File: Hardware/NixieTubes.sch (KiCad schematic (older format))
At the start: 14 parts, among them U1 HV5530, U2 HV5530

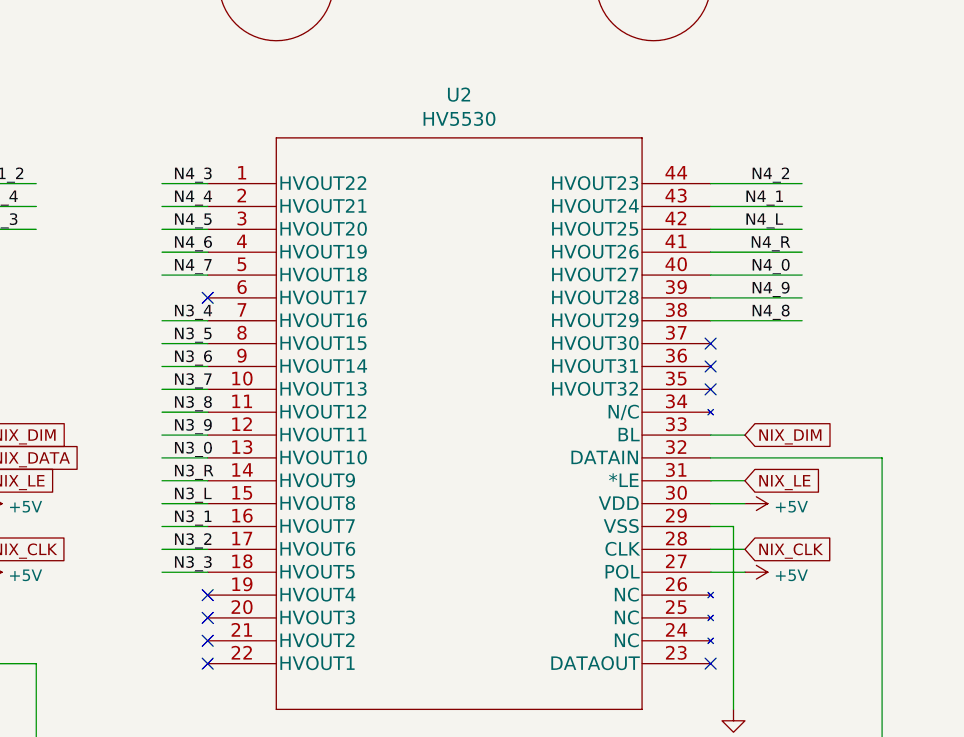
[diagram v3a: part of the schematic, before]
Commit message: Routed right nixies
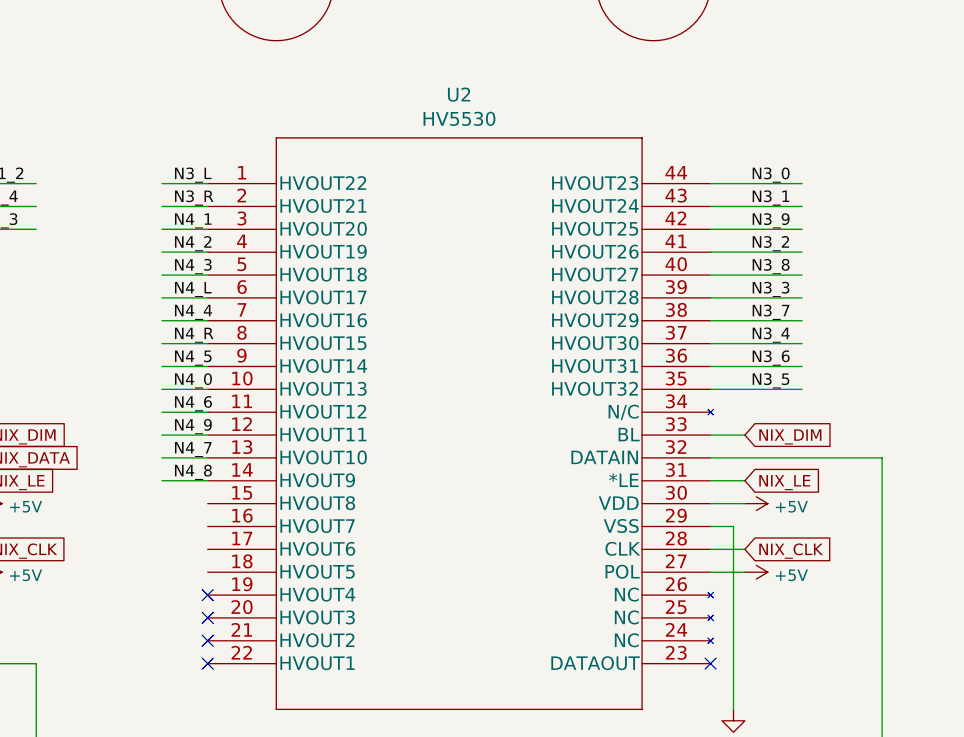
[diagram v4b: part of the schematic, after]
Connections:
- no-connect marks 16 -> 12
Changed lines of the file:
@@
 Wire Wire Line
 	7000 1400 7050 1400
-Wire Wire Line
-	4500 4000 4300 4000
-Wire Wire Line
-	4500 3900 4300 3900
-Wire Wire Line
-	4500 3800 4300 3800
-Wire Wire Line
-	4500 3700 4300 3700
-Wire Wire Line
-	4500 3600 4300 3600
-Wire Wire Line
-	4500 3500 4300 3500
-Wire Wire Line
-	4500 3400 4300 3400
-Wire Wire Line
-	4500 3300 4300 3300
-Wire Wire Line
-	4500 4400 4300 4400
-Wire Wire Line
-	4500 4300 4300 4300
-Wire Wire Line
-	4500 4200 4300 4200
-Wire Wire Line
-	4300 4100 4500 4100
-Text Label 4350 4100 0    50   ~ 0
-N3_L
-Text Label 4350 4200 0    50   ~ 0
-N3_1
-Text Label 4350 4300 0    50   ~ 0
+Text Label 7050 2700 2    50   ~ 0
+N3_0
+Text Label 7050 3300 2    50   ~ 0
+N3_7
+Text Label 7050 3200 2    50   ~ 0
+N3_3
+Text Label 7050 3100 2    50   ~ 0
+N3_8
+Text Label 7050 3000 2    50   ~ 0
 N3_2
-Text Label 4350 4400 0    50   ~ 0
-N3_3
-Text Label 4350 3300 0    50   ~ 0
-N3_4
-Text Label 4350 3400 0    50   ~ 0
-N3_5
-Text Label 4350 3500 0    50   ~ 0
-N3_6
-Text Label 4350 3600 0    50   ~ 0
-N3_7
-Text Label 4350 3700 0    50   ~ 0
-N3_8
-Text Label 4350 3800 0    50   ~ 0
-N3_9
-Text Label 4350 3900 0    50   ~ 0
-N3_0
-Text Label 4350 4000 0    50   ~ 0
-N3_R
-Text Label 7050 2700 2    50   ~ 0
-N4_2
-Text Label 4350 2700 0    50   ~ 0
-N4_3
-Text Label 4350 2800 0    50   ~ 0
-N4_4
-Text Label 4350 2900 0    50   ~ 0
-N4_5
-Text Label 4350 3000 0    50   ~ 0
-N4_6
-Text Label 4350 3100 0    50   ~ 0
-N4_7
-Text Label 7050 3300 2    50   ~ 0
-N4_8
-Text Label 7050 3200 2    50   ~ 0
-N4_9
-Text Label 7050 3100 2    50   ~ 0
-N4_0
-Text Label 7050 3000 2    50   ~ 0
-N4_R
-Text Label 6850 2800 0    50   ~ 0
-N4_1
-Text Label 6850 2900 0    50   ~ 0
-N4_L
-Wire Wire Line
-	6700 2900 7100 2900
-Wire Wire Line
-	6700 2800 7100 2800
 Wire Wire Line
 	6700 3200 7100 3200
 Wire Wire Line
 	6700 3300 7100 3300
-Wire Wire Line
-	4500 3100 4300 3100
-Wire Wire Line
-	4500 3000 4300 3000
-Wire Wire Line
-	4500 2900 4300 2900
-Wire Wire Line
-	4500 2800 4300 2800
-Wire Wire Line
-	4500 2700 4300 2700
 Wire Wire Line
 	6700 2700 7100 2700
@@
 Wire Wire Line
 	6700 3000 7100 3000
-NoConn ~ 6700 3500
-NoConn ~ 6700 3600
-NoConn ~ 4500 3200
 NoConn ~ 4500 4500
 Wire Wire Line
@@
 Wire Wire Line
 	3750 4800 3750 5400
-NoConn ~ 6700 3400
 Wire Wire Line
 	7450 3900 7450 5400
@@
 NoConn ~ 3350 3500
 NoConn ~ 3350 3600
+Text Label 7050 3600 2    50   ~ 0
+N3_5
+Text Label 7050 3500 2    50   ~ 0
+N3_6
+Wire Wire Line
+	6700 3500 7100 3500
+Wire Wire Line
+	6700 3600 7100 3600
+Text Label 7050 3400 2    50   ~ 0
+N3_4
+Wire Wire Line
+	6700 3400 7100 3400
+Text Label 7050 2900 2    50   ~ 0
+N3_9
+Text Label 7050 2800 2    50   ~ 0
+N3_1
+Wire Wire Line
+	6700 2900 7100 2900
+Wire Wire Line
+	6700 2800 7100 2800
+Wire Wire Line
+	4500 3700 4300 3700
+Wire Wire Line
+	4500 3600 4300 3600
+Text Label 4350 3600 0    50   ~ 0
+N4_0
+Text Label 4350 3700 0    50   ~ 0
+N4_6
+Wire Wire Line
+	4500 3500 4300 3500
+Wire Wire Line
+	4500 3400 4300 3400
+Text Label 4350 3000 0    50   ~ 0
+N4_2
+Text Label 4350 3100 0    50   ~ 0
+N4_3
+Text Label 4350 3200 0    50   ~ 0
+N4_L
+Text Label 4350 3300 0    50   ~ 0
+N4_4
+Text Label 4350 3400 0    50   ~ 0
+N4_R
+Text Label 4350 3500 0    50   ~ 0
+N4_5
+Wire Wire Line
+	4500 3300 4300 3300
+Wire Wire Line
+	4500 3200 4300 3200
+Wire Wire Line
+	4500 3100 4300 3100
+Wire Wire Line
+	4500 3000 4300 3000
+Text Label 4350 2700 0    50   ~ 0
+N3_L
+Text Label 4350 2800 0    50   ~ 0
+N3_R
+Text Label 4350 2900 0    50   ~ 0
+N4_1
+Wire Wire Line
+	4500 2900 4300 2900
+Wire Wire Line
+	4500 2800 4300 2800
+Wire Wire Line
+	4500 2700 4300 2700
+Wire Wire Line
+	4500 4000 4300 4000
+Wire Wire Line
+	4500 3900 4300 3900
+Text Label 4350 3900 0    50   ~ 0
+N4_7
+Text Label 4350 4000 0    50   ~ 0
+N4_8
+Wire Wire Line
+	4500 3800 4300 3800
+Text Label 4350 3800 0    50   ~ 0
+N4_9
 $EndSCHEMATC
